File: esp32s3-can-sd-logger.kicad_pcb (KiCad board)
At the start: 4 copper layers, 98 x 90 mm, 163 parts, among them J1 OBD-II harness, J2 DevKit J1, J3 DevKit J3, J4 I2C / Qwiic, J5 WS2812, J6 Rail break-out, J7 microSD push-pull, J8 Sensor harness, J9 Spare diff in, Q1 DMG2301L, Q2 2N7002, Q3 2N7002, U1 TLV431A, U2 74AHCT1G125, U3 SRV05-4, U4 SRV05-4, U5 TJA1051T/3, U6 MCP2518FD, U7 TJA1051T/3, U8 ADS1115 (0x48), U9 ADS1115 (0x49), Y1 40MHz

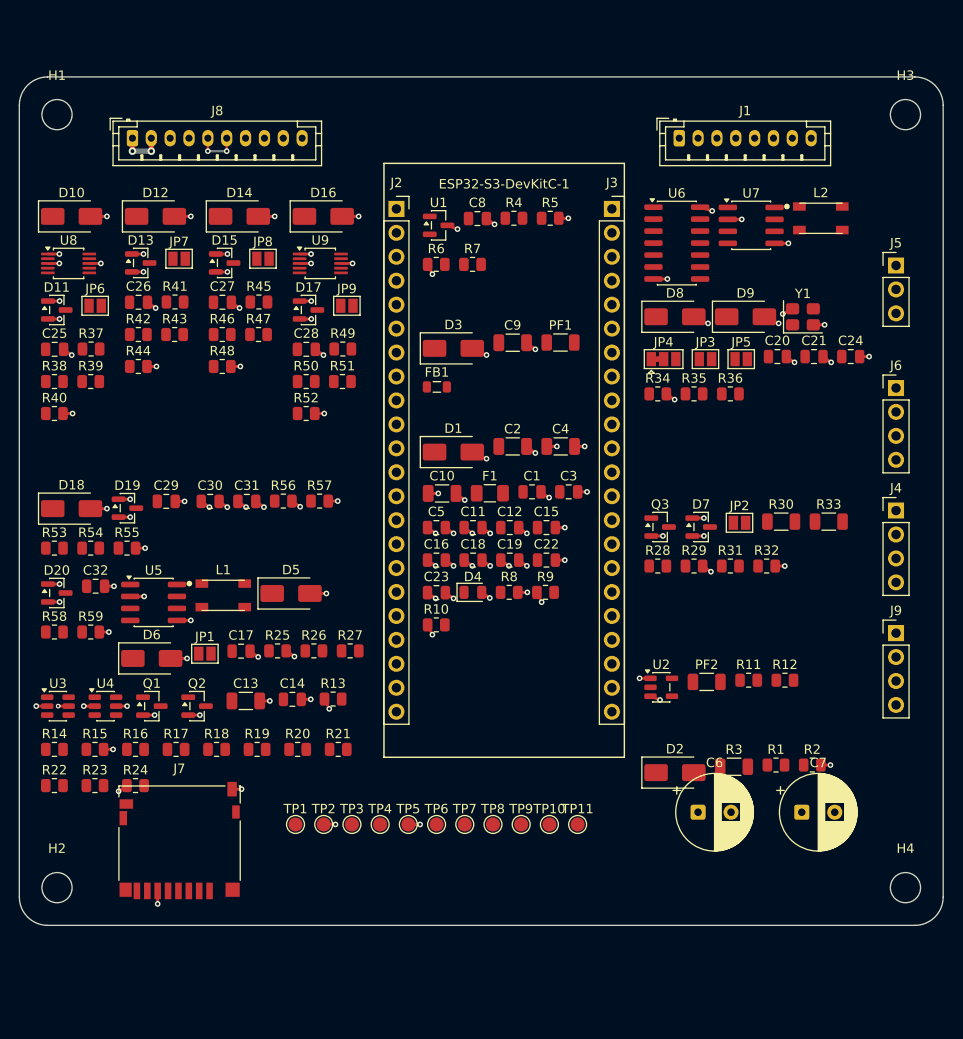
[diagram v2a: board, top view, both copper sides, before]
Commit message: Route, audit and document the carrier; verify every part number against the catalogue
Ordering is the point of this pass, so the part numbers came first. Every
LCSC number on the board was opened and read -- manufacturer part, package,
and the parameter that decides whether it is the right part. That found:

  C2148396 for the MCP2518FD    is an 18.7k resistor, out of stock -> C626759
  C255909  for a 40 MHz crystal is a 16 MHz crystal              -> C5186937
  C157966  for a JST PH 10-way  is a JST XH 9-way, 2.5 mm pitch  -> C158038

Three of the five numbers introduced last sitting were wrong, and all three
were plausible enough that the BOM exported clean. docs/PARTS.md records the
lot, including that LCSC's own listing for the microSD socket claims it has
no card-detect switch -- it has one, and the schematic is right.

Two footprints would not have soldered: both polyfuses are 1812 parts sitting
on a 1206 land, inherited from the parent board where nothing had ever
compared a part's package against its footprint. And the generic-passive
table was keyed on value alone, so the 1206 positions added last sitting
would have ordered 0805 parts -- right resistance, wrong footprint, every
board. It is keyed on (value, package) now and returns nothing rather than
guessing, so an unmatched line has no part number and somebody has to look.

Several values moved to match what is actually stocked: the power-fail
divider to 43k/18k (same trip point to 2 mV, both stocked 1 % parts), the
K-line series and pull-up to 20 R and 750 R, and the supercap charge resistor
from 22 R to 100 R -- 22 R put 1 W into a 250 mW part for the first several
seconds of every power-up.

Two real defects, both found by tools rather than by reading:

  - The hold-up Schottky was BACKWARDS. Reversed it shorts out the inrush
    limiter and blocks the discharge, so the supercap bank could never hold
    the rail up and the whole hold-up circuit was inert. audit_polarity found
    it once its expectat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
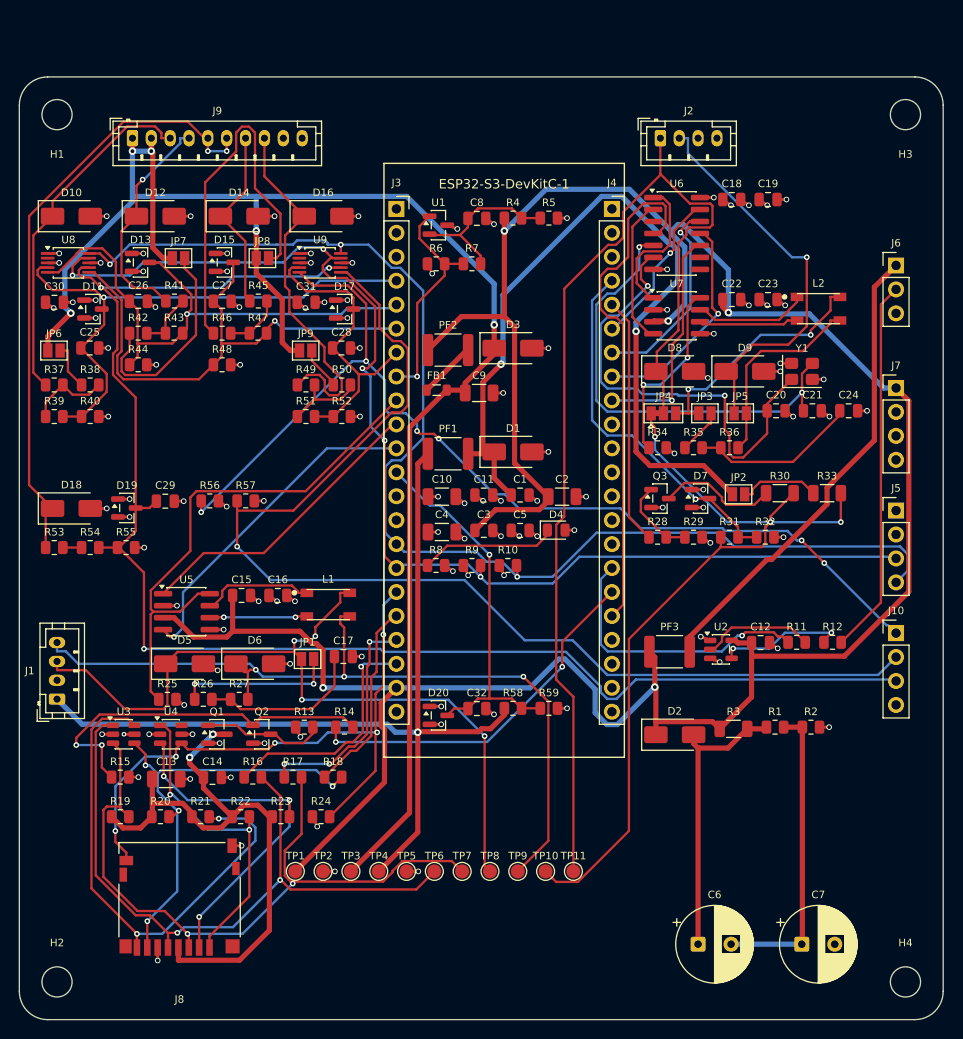
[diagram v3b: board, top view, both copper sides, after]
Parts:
- removed F1: 0.5A slow, Fuse_1206_3216Metric
- added J10: Spare diff in, PinHeader_1x04_P2.54mm_Vertical, F.Cu at (93.0, 59.0)
- added PF3: 0.5A hold, R_1812_4532Metric, F.Cu at (69.0, 61.0)
- C25, C26, C27, C28, C29: value 100nF -> 470nF
- J1: value OBD-II harness -> CAN1 + power harness; footprint JST_PH_B8B-PH-K_1x08_P2.00mm_Vertical -> JST_PH_B4B-PH-K_1x04_P2.00mm_Vertical
- J2: value DevKit J1 -> Aux bus harness; footprint PinSocket_1x22_P2.54mm_Vertical -> JST_PH_B4B-PH-K_1x04_P2.00mm_Vertical
- J3: value DevKit J3 -> DevKit J1
- J4: value I2C / Qwiic -> DevKit J3; footprint PinHeader_1x04_P2.54mm_Vertical -> PinSocket_1x22_P2.54mm_Vertical
- J5: value WS2812 -> I2C / Qwiic; footprint PinHeader_1x03_P2.54mm_Vertical -> PinHeader_1x04_P2.54mm_Vertical
- J6: value Rail break-out -> WS2812; footprint PinHeader_1x04_P2.54mm_Vertical -> PinHeader_1x03_P2.54mm_Vertical
- J7: value microSD push-pull -> Rail break-out; footprint microSD_HC_Hirose_DM3D-SF -> PinHeader_1x04_P2.54mm_Vertical
- J8: value Sensor harness -> microSD push-pull; footprint JST_PH_B10B-PH-K_1x10_P2.00mm_Vertical -> microSD_HC_Hirose_DM3D-SF
- J9: value Spare diff in -> Sensor harness; footprint PinHeader_1x04_P2.54mm_Vertical -> JST_PH_B10B-PH-K_1x10_P2.00mm_Vertical
- PF1: footprint R_1206_3216Metric -> R_1812_4532Metric
- PF2: value 0.5A hold -> 0.2A PTC; footprint R_1206_3216Metric -> R_1812_4532Metric
- R3: value 22 -> 100
- R30: value 33 -> 20
- R33: value 510 -> 750
- R4: value 28.7k -> 43k
- R5: value 12.0k -> 18k
- moved J9 96.5 mm to (12.0, 6.50)
- moved J7 89.9 mm to (93.0, 33.0)
- moved J1 88.9 mm to (4.00, 66.0), turned to 90 degrees
- moved J8 80.7 mm to (17.0, 87.0)
- moved R58 49.3 mm to (52.4, 67.0)
- moved R59 49.3 mm to (56.2, 67.0)
- moved C18 47.1 mm to (75.6, 13.0)
- moved C19 47.1 mm to (79.4, 13.0)
- moved C23 46.9 mm to (79.4, 23.6)
- moved PF2 44.6 mm to (45.5, 29.0)
- moved J4 44.0 mm to (62.9, 14.0)
- moved D20 42.5 mm to (44.5, 67.7)
- moved C32 42.5 mm to (48.5, 67.0)
- moved C22 33.9 mm to (75.6, 23.6)
- moved C15 33.1 mm to (23.6, 55.0)
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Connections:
- D2 pad 1: SCAP_TOP -> +5V
- D2 pad 2: +5V -> SCAP_TOP
- J2 pad 1: +3V3 -> AUX_A
- J2 pad 2: +3V3 -> AUX_B
- J2 pad 3: (no net) -> GND
- J2 pad 4: AIN1 -> GND
- J3 pad 1: GND -> +3V3
- J3 pad 10: (no net) -> CAN_TX
- J3 pad 11: (no net) -> CAN_RX
- J3 pad 12: (no net) -> VBAT_SNS
- J3 pad 15: (no net) -> I2C_SCL
- J3 pad 16: LED_DIN_MCU -> I2C_SDA
- J3 pad 17: SD_PWR_EN -> SD_CD
- J3 pad 18: CAN2_INT -> SD_D0
- J3 pad 19: (no net) -> SD_CMD
- J3 pad 2: (no net) -> +3V3
- J3 pad 20: (no net) -> SD_CLK
- J3 pad 21: GND -> +5V
- J3 pad 4: K_RX -> AIN1
- J3 pad 5: K_TX -> AIN2
- J3 pad 6: CAN2_CS -> AIN3
- J3 pad 7: CAN2_MISO -> AIN4
- J3 pad 8: CAN2_MOSI -> PWR_FAIL
- J3 pad 9: CAN2_SCK -> CAN_S
- J4 pad 2: +3V3 -> (no net)
- J4 pad 3: I2C_SDA -> (no net)
- J4 pad 4: I2C_SCL -> K_RX
- J5 pad 1: LED_5V -> GND
- J5 pad 2: LED_DIN_J -> +3V3
- J5 pad 3: GND -> I2C_SDA
- J6 pad 1: +5V -> LED_5V
- J6 pad 2: +3V3 -> LED_DIN_J
- J7 pad 1: SD_D2_C -> +5V
- J7 pad 2: SD_D3_C -> +3V3
- J7 pad 3: SD_CMD_C -> GND
- J7 pad 4: SD_VDD -> GND
- J8 pad 1: +5VS -> SD_D2_C
- J8 pad 2: +5VS -> SD_D3_C
- J8 pad 3: AIN1_IN -> SD_CMD_C
- J8 pad 4: AIN2_IN -> SD_VDD
- J8 pad 5: SENS_RTN -> SD_CLK_C
- J8 pad 6: SENS_RTN -> GND
- J8 pad 7: AIN3_IN -> SD_D0_C
- J8 pad 8: AIN4_IN -> SD_D1_C
- J8 pad 9: GND -> SD_CD
- J9 pad 1: AIN_SP1 -> +5VS
- J9 pad 2: AIN_SP2 -> +5VS
- J9 pad 3: AGND_SENSE -> AIN1_IN
- J9 pad 4: GND -> AIN2_IN
- PF1 pad 1: +5V -> OBD_VBAT
- PF1 pad 2: VSENS_F -> OBD_VBAT_F
- PF2 pad 2: LED_5V -> VSENS_F
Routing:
- net +5V: track 0.00 -> 284.0 mm, vias 0 -> 5
- net +5VS: track 4.75 -> 174.2 mm, vias 2 -> 5
- net AGND_SENSE: track 0.00 -> 161.0 mm, vias 0 -> 3
- net I2C_SCL: track 0.00 -> 133.1 mm, vias 0 -> 3
- net I2C_SDA: track 0.00 -> 128.7 mm, vias 0 -> 5
- net AIN_SP2: track 0.00 -> 121.8 mm, vias 0 -> 1
- net AUX_A: track 0.00 -> 116.6 mm
- net AIN_SP1: track 0.00 -> 108.7 mm, vias 0 -> 6
- net OBD_VBAT: track 0.00 -> 96.8 mm, vias 0 -> 1
- net K_LINE: track 0.00 -> 88.2 mm, vias 0 -> 3
- net CAN_L: track 0.00 -> 87.7 mm, vias 0 -> 3
- net OBD_VBAT_F: track 0.00 -> 86.2 mm, vias 0 -> 2
- net CAN_H: track 0.00 -> 84.7 mm, vias 0 -> 4
- net SD_CMD_C: track 0.00 -> 75.7 mm, vias 0 -> 2
- net SD_CLK_C: track 0.00 -> 72.4 mm, vias 0 -> 2
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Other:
- board size 98 x 90 mm -> 98 x 100 mm

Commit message: Implement the cost reductions: 1% dividers and a 0.33 F bank -- $18.29 to $13.87
Two of the three changes from docs/COST.md. The third was dropped once I
checked it properly, which is the more interesting half of this commit.

PRECISION RESISTORS TO 1%, saving $2.62 measured. Fifteen 0.1% parts cost
$2.68 -- more than the CAN controller -- to tighten a divider whose error the
ADS1115's own +/-0.30% gain spec already dominates. Absolute scale has to be
calibrated whatever the tolerance, and the thing calibration cannot fix, the
match between the signal chain and the return attenuator, is fine at 1%: a
300 mV chassis offset leaves 6 mV instead of 0.6 mV, both negligible against
the 300 mV being removed.

The lower leg went 2.21k -> 2.2k with it, because E96 values do not exist in
the 1% jellybean library. That is a happy accident: 2.2/13.2 is exactly 1/6,
so DIVIDER_GAIN is a round 6.0000 instead of 5.9774.

HOLD-UP BANK 1 F -> 0.33 F per cell, saving roughly $1.80. 1 F bought 2500 ms
that nothing needs -- the parent board shipped 127 ms and that was judged
adequate, a healthy card flushes in 18 ms, and the worst stall the firmware
studies model is 500 ms. 0.33 F gives 825 ms shed, six times the parent's
margin and still 65% clear of that worst case. The budgets in fwsim, studies
11 and 12 and their sweep ranges all move with it.

THE microSD SWAP IS NOT DONE, and the $1.06 I quoted for it was arithmetic
against a part I could not verify. Those $0.04 sockets are house parts whose
only drawing is a scanned PDF with no extractable dimensions, so the land
pattern cannot be checked -- and shipping an unverified footprint on five
boards to save a dollar is not a trade this project should make. The
verifiable alternatives are worse than the search suggested: the Molex
47219-2001 with a KiCad footprint is $0.63 against the Hirose's $1.12, so the
honest saving is $0.49, and it costs the card-detect signal and swaps a
push-pull for a hinged lid. The Hirose stays. COST.md recor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
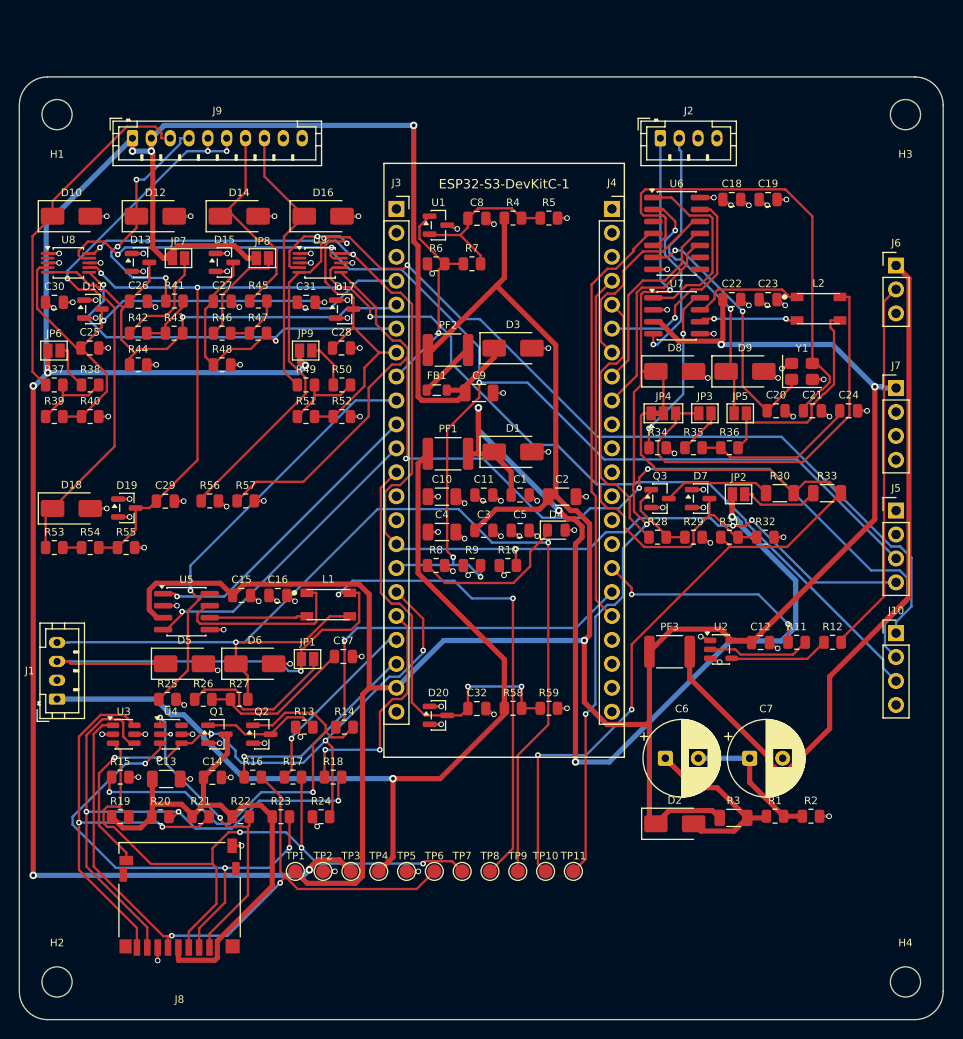
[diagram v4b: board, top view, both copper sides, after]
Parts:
- C6, C7: value 1F -> 0.33F
- R40, R44, R48, R52, R55: value 2.21k -> 2.2k
- moved C7 20.5 mm to (77.5, 72.3)
- moved C6 20.0 mm to (68.5, 72.3)
- moved R1 9.45 mm to (80.2, 78.4)
- moved R2 9.45 mm to (84.0, 78.4)
- moved R3 9.45 mm to (75.8, 78.6)
- moved D2 9.45 mm to (69.5, 79.2)
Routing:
- net +5VS: track 174.2 -> 248.9 mm, vias 5 -> 8
- net AIN3_PU: track 41.0 -> 11.6 mm
- net CAN_L: track 87.7 -> 115.5 mm, vias 3 -> 2
- net LED_5V: track 50.3 -> 77.0 mm
- net AUX_A: track 116.6 -> 92.0 mm, vias 0 -> 3
- net XTAL1: track 49.1 -> 28.5 mm
- net CAN_H: track 84.7 -> 102.8 mm, vias 4 -> 3
- net SD_D0_C: track 47.4 -> 65.5 mm, vias 4 -> 3
- net CAN2_H_C: track 26.3 -> 43.9 mm, vias 2 -> 0
- net SCAP_MID: track 32.5 -> 15.1 mm
- net AGND_SENSE: track 161.0 -> 144.2 mm, vias 3 -> 4
- net OBD_VBAT_F: track 86.2 -> 102.1 mm, vias 2 -> 4
- net SD_D3_C: track 39.4 -> 52.4 mm
- net AIN_SP1: track 108.7 -> 120.6 mm, vias 6 -> 1
- net AIN2_PU: track 22.9 -> 11.6 mm
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
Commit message: Precision where it changes the answer: 0.1% on the two gain-setting resistors
Walking back half of the previous commit, because its argument depended on a
calibration step that is not going to happen. All-1% dividers are only
equivalent to 0.1% if somebody measures each channel against a known voltage
and stores a constant; without that they are 1.67% worst case against 0.167%.

But going straight back to fifteen 0.1% parts would have been the wrong
correction. Gain is Rlow/(Rser+Rup+Rlow), so each resistor moves it in
proportion to its share of the total:

    1k series    0.076 -> 0.076% of gain per 1% of tolerance
    10k upper    0.758 -> 0.758%
    2.21k lower  0.833 -> 0.833%

The series resistor is TEN TIMES less sensitive than the other two, and it
was the most expensive 0.1% part on the board at $0.30 against $0.19 and
$0.05. So it stays 1% and the two that set the ratio go back to 0.1%.

That lands the divider at 0.235% worst case, just under the ADS1115's own
0.30% maximum gain error -- the point past which spending more buys nothing --
and it needs no calibration. $1.21 a board against $2.68 for all-0.1% and
$0.05 for all-1%.

Board is $15.02 against the $18.29 it started at, an 18% cut rather than the
24% the previous commit claimed. DIVIDER_GAIN returns to 5.9774 and the ratio
is 2.21/13.21 again; the exact-1/6 was a nicety of the all-1% build, not a
requirement.

Also adds gen/audit_schematic.py, which measures two things nothing else
looks at: text printed on top of other text, and symbols connected only by
net label with no wire attached. It found its own first bug immediately --
counting the lib_symbols block, where every library definition carries
Reference and Value properties at identical coordinates, as 187 collisions
that do not exist on the drawing.

Verification unchanged: ERC clean, DRC 0 violations 0 unconnected, 50/50
firmware checks, 17/17 mutations, ngspice clean, docs audit clean.
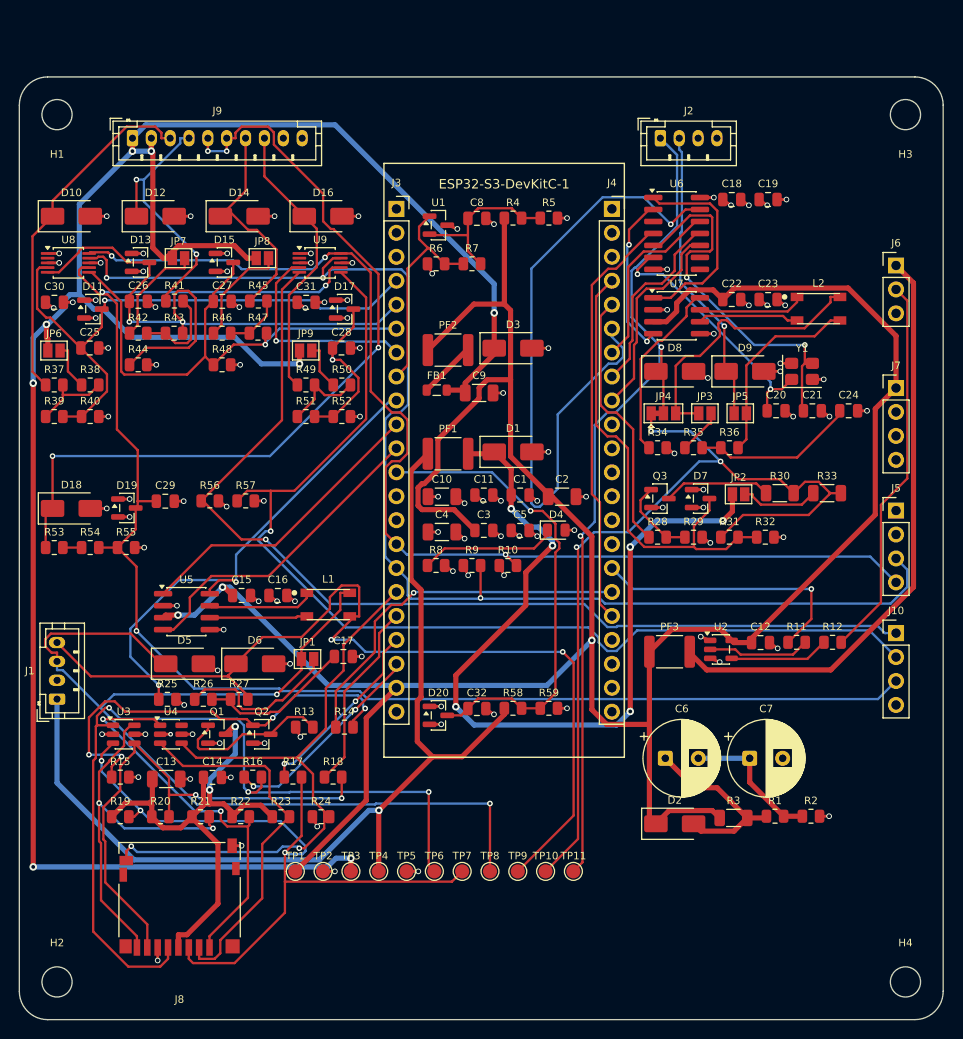
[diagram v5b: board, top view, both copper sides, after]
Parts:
- R40, R44, R48, R52, R55: value 2.2k -> 2.21k
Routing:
- net CAN2_CS: track 22.6 -> 72.3 mm
- net SENS_RTN: track 60.5 -> 87.8 mm, vias 3 -> 4
- net SD_CLK_C: track 72.3 -> 90.3 mm, vias 2 -> 3
- net AIN2: track 53.3 -> 68.8 mm, vias 1 -> 2
- net AGND_SENSE: track 144.2 -> 159.2 mm, vias 4 -> 3
- net CAN_L: track 115.5 -> 100.9 mm
- net LED_5V: track 77.0 -> 63.1 mm
- net CAN2_H_C: track 43.9 -> 30.0 mm
- net OBD_VBAT_F: track 102.1 -> 88.8 mm, vias 4 -> 6
- net +5VS: track 248.9 -> 236.1 mm
- net SD_D3_C: track 52.4 -> 39.8 mm, vias 3 -> 0
- net AIN_SP1: track 120.6 -> 108.1 mm
- net XTAL2: track 51.0 -> 39.8 mm, vias 0 -> 2
- net OBD_VBAT: track 96.3 -> 107.4 mm
- net SD_D0_C: track 65.5 -> 55.0 mm, vias 3 -> 2
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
